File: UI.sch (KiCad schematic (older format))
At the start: 8 parts, among them SW501 SW_Push, SW502 SW_Push

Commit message: Rough PCB layout
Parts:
- added J501, J502: Conn_01x01, MountingHole:MountingHole_3.2mm_M3, symbol Connector_Generic:Conn_01x01
- C501, C502: value 0.1u/50V -> 0.1uF/50V; footprint (none) -> Capacitor_SMD:C_0603_1608Metric
- D501, D502: footprint (none) -> LED_SMD:LED_0603_1608Metric
- R501, R502: footprint (none) -> Resistor_SMD:R_0402_1005Metric
- SW501, SW502: footprint (none) -> Button_Switch_SMD:SW_SPST_TL3342
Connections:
- wire segments 22 -> 24
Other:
- note added: "Mounting holes"
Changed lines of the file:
@@
 F 0 "SW501" H 2100 3335 50  0000 C CNN
 F 1 "SW_Push" H 2100 3244 50  0000 C CNN
-F 2 "" H 2100 3250 50  0001 C CNN
+F 2 "Button_Switch_SMD:SW_SPST_TL3342" H 2100 3250 50  0001 C CNN
 F 3 "~" H 2100 3250 50  0001 C CNN
 	1    2100 3050
@@
 F 0 "SW502" H 2100 4185 50  0000 C CNN
 F 1 "SW_Push" H 2100 4094 50  0000 C CNN
-F 2 "" H 2100 4100 50  0001 C CNN
+F 2 "Button_Switch_SMD:SW_SPST_TL3342" H 2100 4100 50  0001 C CNN
 F 3 "~" H 2100 4100 50  0001 C CNN
 	1    2100 3900
@@
 AR Path="/5FC50B89/5FC5F7FF" Ref="C501"  Part="1"
 F 0 "C501" V 1871 3350 50  0000 C CNN
-F 1 "0.1u/50V" V 1962 3350 50  0000 C CNN
-F 2 "" H 2100 3350 50  0001 C CNN
+F 1 "0.1uF/50V" V 1962 3350 50  0000 C CNN
+F 2 "Capacitor_SMD:C_0603_1608Metric" H 2100 3350 50  0001 C CNN
 F 3 "~" H 2100 3350 50  0001 C CNN
 	1    2100 3350
@@
 AR Path="/5FC50B89/5FC5F805" Ref="C502"  Part="1"
 F 0 "C502" V 1871 4200 50  0000 C CNN
-F 1 "0.1u/50V" V 1962 4200 50  0000 C CNN
-F 2 "" H 2100 4200 50  0001 C CNN
+F 1 "0.1uF/50V" V 1962 4200 50  0000 C CNN
+F 2 "Capacitor_SMD:C_0603_1608Metric" H 2100 4200 50  0001 C CNN
 F 3 "~" H 2100 4200 50  0001 C CNN
 	1    2100 4200
@@
 F 0 "D502" V 2389 1732 50  0000 R CNN
 F 1 "RED LED" V 2298 1732 50  0000 R CNN
-F 2 "" H 2350 1850 50  0001 C CNN
+F 2 "LED_SMD:LED_0603_1608Metric" H 2350 1850 50  0001 C CNN
 F 3 "~" H 2350 1850 50  0001 C CNN
 	1    2350 1850
@@
 F 0 "R502" H 2420 1496 50  0000 L CNN
 F 1 "2k" H 2420 1405 50  0000 L CNN
-F 2 "" V 2280 1450 50  0001 C CNN
+F 2 "Resistor_SMD:R_0402_1005Metric" V 2280 1450 50  0001 C CNN
 F 3 "~" H 2350 1450 50  0001 C CNN
 	1    2350 1450
@@
 F 0 "D501" V 1789 1732 50  0000 R CNN
 F 1 "BLUE LED" V 1698 1732 50  0000 R CNN
-F 2 "" H 1750 1850 50  0001 C CNN
+F 2 "LED_SMD:LED_0603_1608Metric" H 1750 1850 50  0001 C CNN
 F 3 "~" H 1750 1850 50  0001 C CNN
 	1    1750 1850
@@
 F 0 "R501" H 1820 1496 50  0000 L CNN
 F 1 "2k" H 1820 1405 50  0000 L CNN
-F 2 "" V 1680 1450 50  0001 C CNN
+F 2 "Resistor_SMD:R_0402_1005Metric" V 1680 1450 50  0001 C CNN
 F 3 "~" H 1750 1450 50  0001 C CNN
 	1    1750 1450
@@
 Text HLabel 1750 1200 1    50   Input ~ 0
 LED
+$Comp
+L Connector_Generic:Conn_01x01 J501
+U 1 1 5F9CE7EE
+P 4050 1200
+F 0 "J501" H 4130 1242 50  0000 L CNN
+F 1 "Conn_01x01" H 4130 1151 50  0000 L CNN
+F 2 "MountingHole:MountingHole_3.2mm_M3" H 4050 1200 50  0001 C CNN
+F 3 "~" H 4050 1200 50  0001 C CNN
+	1    4050 1200
+	1    0    0    -1
+$EndComp
+$Comp
+L Connector_Generic:Conn_01x01 J502
+U 1 1 5F9CF747
+P 4050 1450
+F 0 "J502" H 4130 1492 50  0000 L CNN
+F 1 "Conn_01x01" H 4130 1401 50  0000 L CNN
+F 2 "MountingHole:MountingHole_3.2mm_M3" H 4050 1450 50  0001 C CNN
+F 3 "~" H 4050 1450 50  0001 C CNN
+	1    4050 1450
+	1    0    0    -1
+$EndComp
+$Comp
+L power:GND #PWR0104
+U 1 1 5F9D0612
+P 3850 2150
+F 0 "#PWR0104" H 3850 1900 50  0001 C CNN
+F 1 "GND" H 3855 1977 50  0000 C CNN
+F 2 "" H 3850 2150 50  0001 C CNN
+F 3 "" H 3850 2150 50  0001 C CNN
+	1    3850 2150
+	1    0    0    -1
+$EndComp
+Connection ~ 3850 1450
+Wire Wire Line
+	3850 1450 3850 1200
+Text Notes 3850 950  0    50   ~ 0
+Mounting holes
+Wire Wire Line
+	3850 1450 3850 2150
 $EndSCHEMATC

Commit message: First attempt at full routing
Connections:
- wire segments 24 -> 22
- no-connect marks 0 -> 2
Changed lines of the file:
@@
 	1    0    0    -1
 $EndComp
-$Comp
-L power:GND #PWR0104
-U 1 1 5F9D0612
-P 3850 2150
-F 0 "#PWR0104" H 3850 1900 50  0001 C CNN
-F 1 "GND" H 3855 1977 50  0000 C CNN
-F 2 "" H 3850 2150 50  0001 C CNN
-F 3 "" H 3850 2150 50  0001 C CNN
-	1    3850 2150
-	1    0    0    -1
-$EndComp
-Connection ~ 3850 1450
-Wire Wire Line
-	3850 1450 3850 1200
 Text Notes 3850 950  0    50   ~ 0
 Mounting holes
-Wire Wire Line
-	3850 1450 3850 2150
+NoConn ~ 3850 1450
+NoConn ~ 3850 1200
 $EndSCHEMATC

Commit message: Specified JLCPCB footprints for components
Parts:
- removed J501, J502: Conn_01x01, MountingHole:MountingHole_3.2mm_M3, symbol Connector_Generic:Conn_01x01
- added H501, H502: MountingHole, SH-ESP32:MountingHole_3.2mm_M3_Unplated, symbol Mechanical:MountingHole
- C501, C502: value 0.1uF/50V -> 100nF/50V; LCSC (none) -> C14663
- D501: LCSC (none) -> C72041
- D502: LCSC (none) -> C2286
- R501, R502: LCSC (none) -> C4109
- SW501, SW502: LCSC (none) -> C318887
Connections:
- no-connect marks 2 -> 0
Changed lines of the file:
@@
 F 2 "Button_Switch_SMD:SW_SPST_TL3342" H 2100 3250 50  0001 C CNN
 F 3 "~" H 2100 3250 50  0001 C CNN
+F 4 "C318887" H 2100 3050 50  0001 C CNN "LCSC"
 	1    2100 3050
 	1    0    0    -1
@@
 F 2 "Button_Switch_SMD:SW_SPST_TL3342" H 2100 4100 50  0001 C CNN
 F 3 "~" H 2100 4100 50  0001 C CNN
+F 4 "C318887" H 2100 3900 50  0001 C CNN "LCSC"
 	1    2100 3900
 	1    0    0    -1
@@
 AR Path="/5FC50B89/5FC5F7FF" Ref="C501"  Part="1"
 F 0 "C501" V 1871 3350 50  0000 C CNN
-F 1 "0.1uF/50V" V 1962 3350 50  0000 C CNN
+F 1 "100nF/50V" V 1962 3350 50  0000 C CNN
 F 2 "Capacitor_SMD:C_0603_1608Metric" H 2100 3350 50  0001 C CNN
 F 3 "~" H 2100 3350 50  0001 C CNN
+F 4 "C14663" H 2100 3350 50  0001 C CNN "LCSC"
 	1    2100 3350
 	0    1    1    0
@@
 AR Path="/5FC50B89/5FC5F805" Ref="C502"  Part="1"
 F 0 "C502" V 1871 4200 50  0000 C CNN
-F 1 "0.1uF/50V" V 1962 4200 50  0000 C CNN
+F 1 "100nF/50V" V 1962 4200 50  0000 C CNN
 F 2 "Capacitor_SMD:C_0603_1608Metric" H 2100 4200 50  0001 C CNN
 F 3 "~" H 2100 4200 50  0001 C CNN
+F 4 "C14663" H 2100 4200 50  0001 C CNN "LCSC"
 	1    2100 4200
 	0    1    1    0
@@
 F 2 "LED_SMD:LED_0603_1608Metric" H 2350 1850 50  0001 C CNN
 F 3 "~" H 2350 1850 50  0001 C CNN
+F 4 "C2286" H 2350 1850 50  0001 C CNN "LCSC"
 	1    2350 1850
 	0    -1   -1   0
@@
 F 2 "Resistor_SMD:R_0402_1005Metric" V 2280 1450 50  0001 C CNN
 F 3 "~" H 2350 1450 50  0001 C CNN
+F 4 "C4109" H 2350 1450 50  0001 C CNN "LCSC"
 	1    2350 1450
 	1    0    0    -1
@@
 F 2 "LED_SMD:LED_0603_1608Metric" H 1750 1850 50  0001 C CNN
 F 3 "~" H 1750 1850 50  0001 C CNN
+F 4 "C72041" H 1750 1850 50  0001 C CNN "LCSC"
 	1    1750 1850
 	0    -1   -1   0
@@
 F 2 "Resistor_SMD:R_0402_1005Metric" V 1680 1450 50  0001 C CNN
 F 3 "~" H 1750 1450 50  0001 C CNN
+F 4 "C4109" H 1750 1450 50  0001 C CNN "LCSC"
 	1    1750 1450
 	1    0    0    -1
@@
 Text HLabel 1750 1200 1    50   Input ~ 0
 LED
-$Comp
-L Connector_Generic:Conn_01x01 J501
-U 1 1 5F9CE7EE
-P 4050 1200
-F 0 "J501" H 4130 1242 50  0000 L CNN
-F 1 "Conn_01x01" H 4130 1151 50  0000 L CNN
-F 2 "MountingHole:MountingHole_3.2mm_M3" H 4050 1200 50  0001 C CNN
-F 3 "~" H 4050 1200 50  0001 C CNN
-	1    4050 1200
-	1    0    0    -1
-$EndComp
-$Comp
-L Connector_Generic:Conn_01x01 J502
-U 1 1 5F9CF747
-P 4050 1450
-F 0 "J502" H 4130 1492 50  0000 L CNN
-F 1 "Conn_01x01" H 4130 1401 50  0000 L CNN
-F 2 "MountingHole:MountingHole_3.2mm_M3" H 4050 1450 50  0001 C CNN
-F 3 "~" H 4050 1450 50  0001 C CNN
-	1    4050 1450
-	1    0    0    -1
-$EndComp
 Text Notes 3850 950  0    50   ~ 0
 Mounting holes
-NoConn ~ 3850 1450
-NoConn ~ 3850 1200
+$Comp
+L Mechanical:MountingHole H501
+U 1 1 5FAE48D5
+P 4150 1200
+F 0 "H501" H 4250 1246 50  0000 L CNN
+F 1 "MountingHole" H 4250 1155 50  0000 L CNN
+F 2 "SH-ESP32:MountingHole_3.2mm_M3_Unplated" H 4150 1200 50  0001 C CNN
+F 3 "~" H 4150 1200 50  0001 C CNN
+	1    4150 1200
+	1    0    0    -1
+$EndComp
+$Comp
+L Mechanical:MountingHole H502
+U 1 1 5FAE4D95
+P 4150 1500
+F 0 "H502" H 4250 1546 50  0000 L CNN
+F 1 "MountingHole" H 4250 1455 50  0000 L CNN
+F 2 "SH-ESP32:MountingHole_3.2mm_M3_Unplated" H 4150 1500 50  0001 C CNN
+F 3 "~" H 4150 1500 50  0001 C CNN
+	1    4150 1500
+	1    0    0    -1
+$EndComp
 $EndSCHEMATC

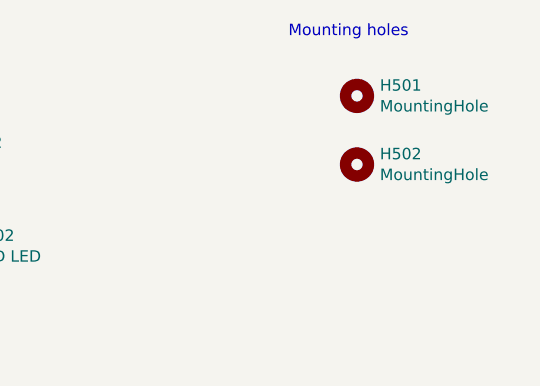
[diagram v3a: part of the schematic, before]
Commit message: Added decoupling caps next to trace vias and copper fill islands
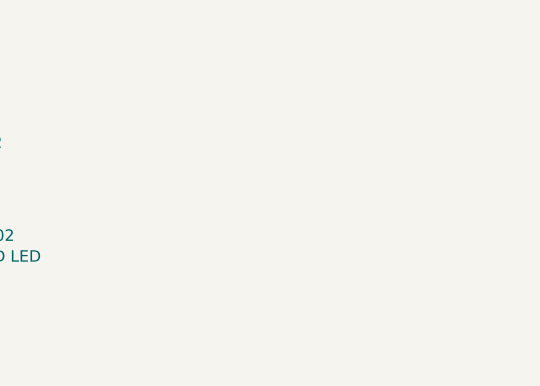
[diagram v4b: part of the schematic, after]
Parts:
- removed H501, H502: MountingHole, SH-ESP32:MountingHole_3.2mm_M3_Unplated, symbol Mechanical:MountingHole
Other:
- note removed: "Mounting holes"
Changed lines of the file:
@@
 $Descr A4 11693 8268
 encoding utf-8
-Sheet 5 9
+Sheet 5 10
 Title "Sailor Hat for ESP32"
 Date ""
@@
 Text HLabel 1750 1200 1    50   Input ~ 0
 LED
-Text Notes 3850 950  0    50   ~ 0
-Mounting holes
-$Comp
-L Mechanical:MountingHole H501
-U 1 1 5FAE48D5
-P 4150 1200
-F 0 "H501" H 4250 1246 50  0000 L CNN
-F 1 "MountingHole" H 4250 1155 50  0000 L CNN
-F 2 "SH-ESP32:MountingHole_3.2mm_M3_Unplated" H 4150 1200 50  0001 C CNN
-F 3 "~" H 4150 1200 50  0001 C CNN
-	1    4150 1200
-	1    0    0    -1
-$EndComp
-$Comp
-L Mechanical:MountingHole H502
-U 1 1 5FAE4D95
-P 4150 1500
-F 0 "H502" H 4250 1546 50  0000 L CNN
-F 1 "MountingHole" H 4250 1455 50  0000 L CNN
-F 2 "SH-ESP32:MountingHole_3.2mm_M3_Unplated" H 4150 1500 50  0001 C CNN
-F 3 "~" H 4150 1500 50  0001 C CNN
-	1    4150 1500
-	1    0    0    -1
-$EndComp
 $EndSCHEMATC

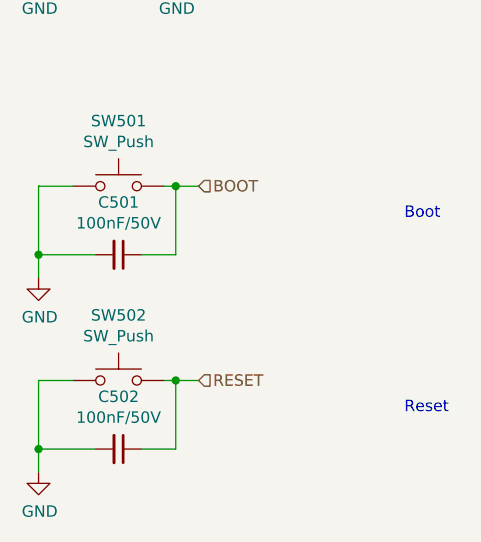
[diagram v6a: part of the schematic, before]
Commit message: Initial version with 40Pin header for Ethernet and re-route.
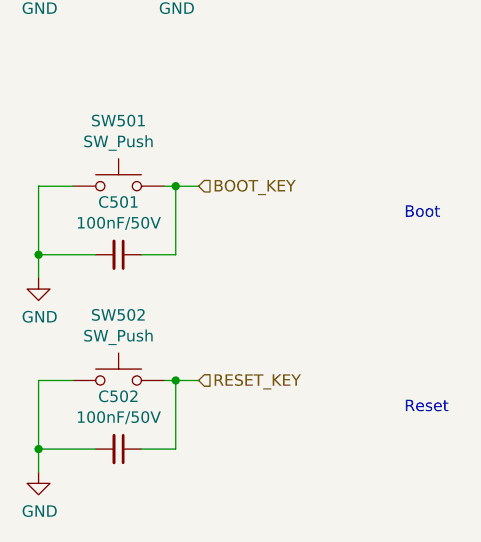
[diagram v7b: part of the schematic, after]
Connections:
- net BOOT renamed BOOT_KEY
- net RESET renamed RESET_KEY
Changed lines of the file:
@@
 	1750 2100 1750 2000
 Text HLabel 2450 3900 2    50   Input ~ 0
-RESET
+RESET_KEY
 Text HLabel 2450 3050 2    50   Input ~ 0
-BOOT
+BOOT_KEY
 Text HLabel 1750 1200 1    50   Input ~ 0
 LED
